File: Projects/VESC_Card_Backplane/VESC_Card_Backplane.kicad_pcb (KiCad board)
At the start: 2 copper layers, 82 x 131 mm, 202 parts, among them M1 FE1.1S, P1 USB_OTG, P10 AMP17614426-2_EDGE, P11 CONN_01X06, P12 CONN_01X02, P13 CONN_01X02, P14 CONN_01X02, P2 EC90_Flat, P3 AMP17614426-2_EDGE, P4 CONN_01X06, P5 CONN_01X04, P5V1 CONN_01X02, P6 EC90_Flat, P7 AMP17614426-2_EDGE, P8 CONN_01X06, P9 EC90_Flat

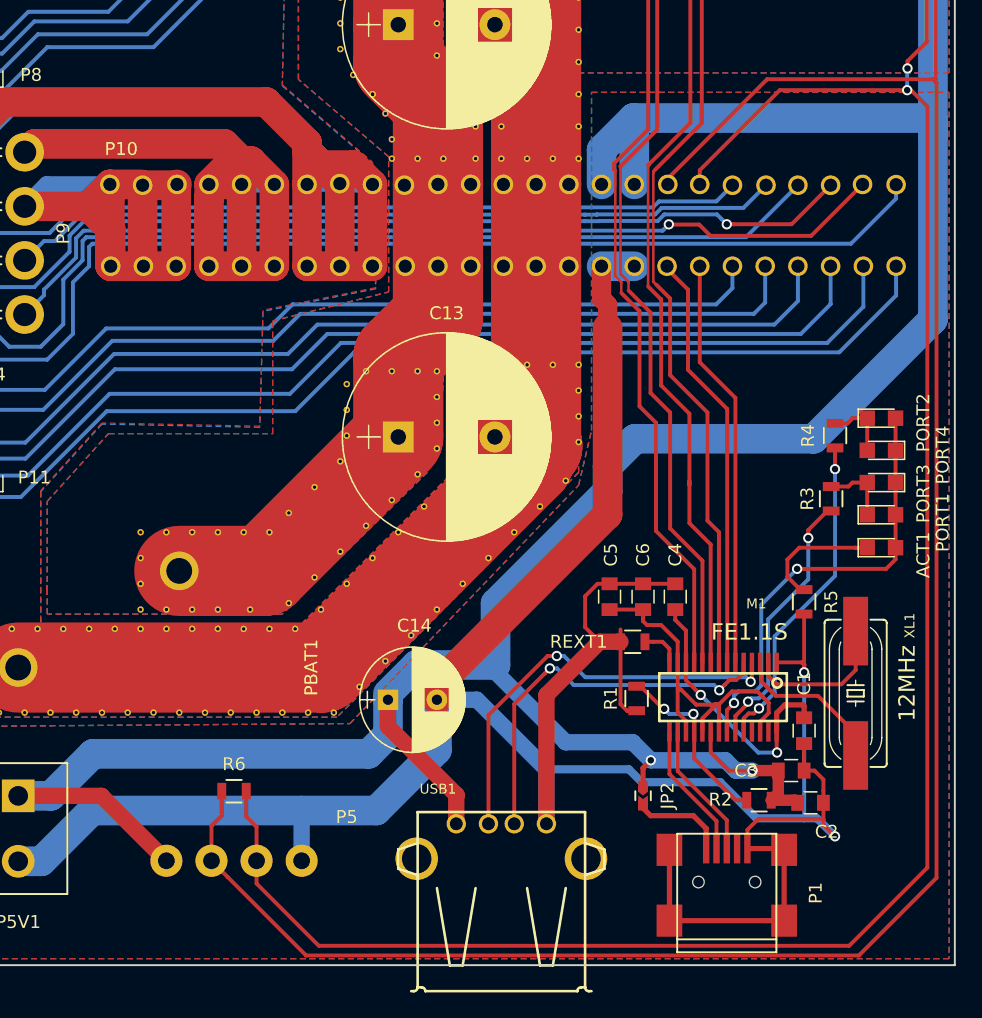
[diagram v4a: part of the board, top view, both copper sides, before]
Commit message: Finished connecting the components, just need to fix copper zones
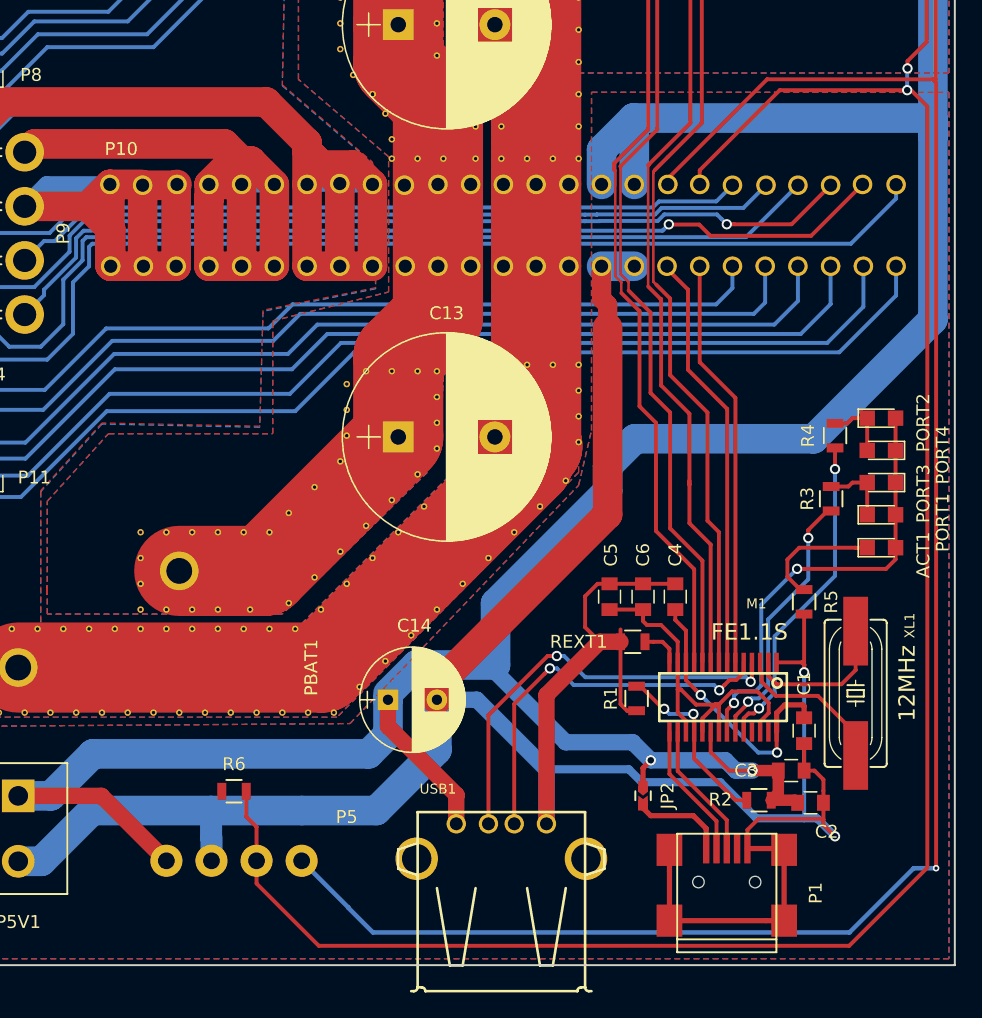
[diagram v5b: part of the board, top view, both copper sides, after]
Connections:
- P5 pad 2: /CANH -> GND
- P5 pad 4: GND -> /CANH
- R6 pad 1: /CANH -> GND
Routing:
- net /CANH: track 261.8 -> 247.1 mm, vias 0 -> 1
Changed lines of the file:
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@@
-(kicad_pcb (version 4) (host pcbnew 4.0.5)
+(kicad_pcb (version 4) (host pcbnew 4.0.4-stable)
   (general
-    (links 416)
-    (no_connects 41)
+    (links 382)
+    (no_connects 7)
     (area 28.124999 14.524999 110.275001 145.675001)
     (thickness 1.6)
     (drawings 8)
-    (tracks 1061)
+    (tracks 1064)
     (zones 0)
     (modules 202)
@@
       (net 3 +5V))
     (pad 2 thru_hole circle (at 3.5 0) (size 2.5 2.5) (drill 1.3) (layers *.Cu *.Mask)
-      (net 32 /CANH))
+      (net 2 GND))
     (pad 3 thru_hole circle (at 7 0) (size 2.5 2.5) (drill 1.3) (layers *.Cu *.Mask)
       (net 33 /CAN_Bus/CANL))
     (pad 4 thru_hole circle (at 10.5 0) (size 2.5 2.5) (drill 1.3) (layers *.Cu *.Mask)
-      (net 2 GND))
+      (net 32 /CANH))
   )
   (module USST-footprints:Molex_39531_1002 (layer F.Cu)
@@
     (fp_line (start -0.6 -0.875) (end 0.6 -0.875) (layer F.SilkS) (width 0.15))
     (pad 1 smd rect (at -0.95 0) (size 0.7 1.3) (layers F.Cu F.Paste F.Mask)
-      (net 32 /CANH))
+      (net 2 GND))
     (pad 2 smd rect (at 0.95 0) (size 0.7 1.3) (layers F.Cu F.Paste F.Mask)
       (net 33 /CAN_Bus/CANL))
@@
   (segment (start 98.4064 125.4) (end 98.5 125.4936) (width 0.4064) (layer F.Cu) (net 1))
   (segment (start 98.5 125.4936) (end 98.5 126.4) (width 0.4064) (layer F.Cu) (net 1))
+  (segment (start 43.236051 133.6) (end 52.47 133.6) (width 2.3) (layer B.Cu) (net 2))
+  (segment (start 52.5 137.5) (end 52.5 135.732234) (width 1.71) (layer B.Cu) (net 2))
+  (segment (start 52.47 133.6) (end 59.5 133.6) (width 2.3) (layer B.Cu) (net 2))
+  (segment (start 52.5 135.732234) (end 52.47 135.702234) (width 1.27) (layer B.Cu) (net 2))
+  (segment (start 52.47 135.702234) (end 52.47 133.6) (width 1.71) (layer B.Cu) (net 2))
   (segment (start 83.25 94.35) (end 82.78 93.88) (width 1.5) (layer F.Cu) (net 2))
   (segment (start 82.78 93.88) (end 82.78 91.35) (width 1.5) (layer F.Cu) (net 2))
@@
   (segment (start 65.3 133.6) (end 70 128.9) (width 2.3) (layer B.Cu) (net 2))
   (segment (start 59.5 133.6) (end 65.3 133.6) (width 2.3) (layer B.Cu) (net 2))
-  (segment (start 43.236051 133.6) (end 59.5 133.6) (width 2.3) (layer B.Cu) (net 2))
   (segment (start 39.296051 137.54) (end 43.236051 133.6) (width 2.3) (layer B.Cu) (net 2))
   (segment (start 37.5 137.54) (end 39.296051 137.54) (width 2.3) (layer B.Cu) (net 2))
@@
   (segment (start 84.25 125.343227) (end 84.756773 125.85) (width 0.3048) (layer F.Cu) (net 2))
   (segment (start 84.756773 125.85) (end 85.5 125.85) (width 0.3048) (layer F.Cu) (net 2))
-  (segment (start 59.5 133.6) (end 59.5 137.5) (width 1.27) (layer B.Cu) (net 2))
   (segment (start 78.5001 130.4001) (end 73.1 125) (width 1.27) (layer B.Cu) (net 2))
   (segment (start 73.1 125) (end 70 125) (width 1.27) (layer B.Cu) (net 2))
@@
   (segment (start 57.5 28.85) (end 57.5 22.5) (width 2.3) (layer F.Cu) (net 31))
   (segment (start 54.96 28.85) (end 54.96 22.5) (width 2.3) (layer F.Cu) (net 31))
-  (segment (start 108.5 76.8385) (end 108.778457 77.116957) (width 0.3048) (layer F.Cu) (net 32))
-  (segment (start 108.778457 77.116957) (end 108.778457 138.821543) (width 0.3048) (layer F.Cu) (net 32))
-  (segment (start 108.778457 138.821543) (end 102.75 144.85) (width 0.3048) (layer F.Cu) (net 32))
-  (segment (start 102.75 144.85) (end 59.85 144.85) (width 0.3048) (layer F.Cu) (net 32))
-  (segment (start 59.85 144.85) (end 53.749999 138.749999) (width 0.3048) (layer F.Cu) (net 32))
-  (segment (start 53.749999 138.749999) (end 52.5 137.5) (width 0.3048) (layer F.Cu) (net 32))
+  (segment (start 108.744286 138.077126) (end 107.007126 138.077126) (width 0.35) (layer B.Cu) (net 32))
+  (segment (start 107.007126 138.077126) (end 102.024252 143.06) (width 0.35) (layer B.Cu) (net 32))
+  (segment (start 102.024252 143.06) (end 65.034652 143.06) (width 0.35) (layer B.Cu) (net 32))
+  (segment (start 63.11815 141.11815) (end 59.5 137.5) (width 0.35) (layer B.Cu) (net 32))
+  (segment (start 65.034652 143.06) (end 63.11815 141.143498) (width 0.35) (layer B.Cu) (net 32))
+  (segment (start 63.11815 141.143498) (end 63.11815 141.11815) (width 0.35) (layer B.Cu) (net 32))
+  (via (at 108.744286 138.077126) (size 0.508) (drill 0.254) (layers F.Cu B.Cu) (net 32))
+  (segment (start 108.5 76.8385) (end 108.744286 77.082786) (width 0.3048) (layer F.Cu) (net 32))
+  (segment (start 108.744286 77.082786) (end 108.744286 138.077126) (width 0.3048) (layer F.Cu) (net 32))
   (segment (start 108.5 76.8385) (end 108.716735 76.8385) (width 0.3048) (layer F.Cu) (net 32))
   (segment (start 108.716735 76.8385) (end 108.716735 48.85) (width 0.3048) (layer F.Cu) (net 32))
@@
   (segment (start 87.9235 84.546156) (end 95.631156 76.8385) (width 0.3048) (layer F.Cu) (net 32))
   (segment (start 95.631156 76.8385) (end 108.5 76.8385) (width 0.3048) (layer F.Cu) (net 32))
-  (segment (start 52.5 137.5) (end 52.5 134.8) (width 0.3048) (layer F.Cu) (net 32))
-  (segment (start 52.5 134.8) (end 53.3 134) (width 0.3048) (layer F.Cu) (net 32))
-  (segment (start 53.3 134) (end 53.3 132.1) (width 0.3048) (layer F.Cu) (net 32))
   (segment (start 90.4 85) (end 90.4 83.896797) (width 0.3048) (layer F.Cu) (net 33))
   (segment (start 90.4 83.896797) (end 96.612047 77.68475) (width 0.3048) (layer F.Cu) (net 33))

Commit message: sync for working with liz
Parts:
- added G***: LOGO, USST-footprints:USSTLOGO, F.Cu at (94.8, 39.2)
- added G***: LOGO, USST-footprints:OSH_PARK_LOGO_SM, F.Cu at (107.5, 134.6)
- added REF**: VIA_STICH_0.5, USST-footprints:VIA_STICH_0.5, F.Cu at (67.5, 20.5)
- added REF**: VIA_STICH_0.5, USST-footprints:VIA_STICH_0.5, F.Cu at (73.2, 50.5)
- added REF**: VIA_STICH_0.5, USST-footprints:VIA_STICH_0.5, F.Cu at (73.2, 49.2)
- added REF**: VIA_STICH_0.5, USST-footprints:VIA_STICH_0.5, F.Cu at (72.2, 48.0)
- added REF**: VIA_STICH_0.5, USST-footprints:VIA_STICH_0.5, F.Cu at (71.2, 46.8)
- added REF**: VIA_STICH_0.5, USST-footprints:VIA_STICH_0.5, F.Cu at (70.0, 45.5)
- added REF**: VIA_STICH_0.5, USST-footprints:VIA_STICH_0.5, F.Cu at (70.0, 44.0)
- added REF**: VIA_STICH_0.5, USST-footprints:VIA_STICH_0.5, F.Cu at (70.0, 42.5)
- added REF**: VIA_STICH_0.5, USST-footprints:VIA_STICH_0.5, F.Cu at (70.0, 40.8)
- added REF**: VIA_STICH_0.5, USST-footprints:VIA_STICH_0.5, F.Cu at (70.0, 39.2)
- added REF**: VIA_STICH_0.5, USST-footprints:VIA_STICH_0.5, F.Cu at (71.2, 38.0)
- added REF**: VIA_STICH_0.5, USST-footprints:VIA_STICH_0.5, F.Cu at (69.5, 20.5)
- added REF**: VIA_STICH_0.5, USST-footprints:VIA_STICH_0.5, F.Cu at (72.5, 36.8)
- added REF**: VIA_STICH_0.5, USST-footprints:VIA_STICH_0.5, F.Cu at (73.2, 35.5)
- added REF**: VIA_STICH_0.5, USST-footprints:VIA_STICH_0.5, F.Cu at (71.0, 35.5)
- added REF**: VIA_STICH_0.5, USST-footprints:VIA_STICH_0.5, F.Cu at (69.5, 35.5)
- added REF**: VIA_STICH_0.5, USST-footprints:VIA_STICH_0.5, F.Cu at (67.5, 35.5)
- added REF**: VIA_STICH_0.5, USST-footprints:VIA_STICH_0.5, F.Cu at (65.8, 35.5)
- added REF**: VIA_STICH_0.5, USST-footprints:VIA_STICH_0.5, F.Cu at (64.0, 36.5)
- added REF**: VIA_STICH_0.5, USST-footprints:VIA_STICH_0.5, F.Cu at (62.2, 37.5)
- added REF**: VIA_STICH_0.5, USST-footprints:VIA_STICH_0.5, F.Cu at (61.0, 38.5)
- added REF**: VIA_STICH_0.5, USST-footprints:VIA_STICH_0.5, F.Cu at (60.0, 39.8)
- added REF**: VIA_STICH_0.5, USST-footprints:VIA_STICH_0.5, F.Cu at (71.2, 20.5)
- added REF**: VIA_STICH_0.5, USST-footprints:VIA_STICH_0.5, F.Cu at (60.0, 41.2)
- added REF**: VIA_STICH_0.5, USST-footprints:VIA_STICH_0.5, F.Cu at (60.0, 42.5)
- added REF**: VIA_STICH_0.5, USST-footprints:VIA_STICH_0.5, F.Cu at (60.0, 44.0)
- added REF**: VIA_STICH_0.5, USST-footprints:VIA_STICH_0.5, F.Cu at (60.0, 45.5)
- added REF**: VIA_STICH_0.5, USST-footprints:VIA_STICH_0.5, F.Cu at (61.2, 46.8)
- added REF**: VIA_STICH_0.5, USST-footprints:VIA_STICH_0.5, F.Cu at (62.5, 48.0)
- added REF**: VIA_STICH_0.5, USST-footprints:VIA_STICH_0.5, F.Cu at (64.0, 49.2)
- added REF**: VIA_STICH_0.5, USST-footprints:VIA_STICH_0.5, F.Cu at (65.2, 50.5)
- added REF**: VIA_STICH_0.5, USST-footprints:VIA_STICH_0.5, F.Cu at (66.8, 51.8)
- added REF**: VIA_STICH_0.5, USST-footprints:VIA_STICH_0.5, F.Cu at (67.5, 53.0)
- added REF**: VIA_STICH_0.5, USST-footprints:VIA_STICH_0.5, F.Cu at (73.0, 20.5)
- added REF**: VIA_STICH_0.5, USST-footprints:VIA_STICH_0.5, F.Cu at (69.5, 53.0)
- added REF**: VIA_STICH_0.5, USST-footprints:VIA_STICH_0.5, F.Cu at (71.2, 53.0)
- added REF**: VIA_STICH_0.5, USST-footprints:VIA_STICH_0.5, F.Cu at (73.0, 53.0)
- added REF**: VIA_STICH_0.5, USST-footprints:VIA_STICH_0.5, F.Cu at (67.5, 62.8)
- added REF**: VIA_STICH_0.5, USST-footprints:VIA_STICH_0.5, F.Cu at (69.0, 62.8)
- added REF**: VIA_STICH_0.5, USST-footprints:VIA_STICH_0.5, F.Cu at (70.2, 62.8)
- added REF**: VIA_STICH_0.5, USST-footprints:VIA_STICH_0.5, F.Cu at (71.5, 62.8)
- added REF**: VIA_STICH_0.5, USST-footprints:VIA_STICH_0.5, F.Cu at (72.8, 62.8)
- added REF**: VIA_STICH_0.5, USST-footprints:VIA_STICH_0.5, F.Cu at (67.2, 30.5)
- added REF**: VIA_STICH_0.5, USST-footprints:VIA_STICH_0.5, F.Cu at (69.0, 30.5)
- added REF**: VIA_STICH_0.5, USST-footprints:VIA_STICH_0.5, F.Cu at (71.0, 30.5)
- added REF**: VIA_STICH_0.5, USST-footprints:VIA_STICH_0.5, F.Cu at (72.8, 30.5)
- added REF**: VIA_STICH_0.5, USST-footprints:VIA_STICH_0.5, F.Cu at (73.2, 51.8)
- moved R6 3.31 mm to (57.5, 132.8)
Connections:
- R6 pad 1: GND -> /CAN_Bus/CANL
- R6 pad 2: /CAN_Bus/CANL -> /CANH
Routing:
- net /CANH: track 247.1 -> 255.0 mm
- net /CAN_Bus/CANL: track 246.1 -> 247.3 mm, vias 4 -> 5
- net /Motor_Controller_C/H3: track 71.1 -> 71.8 mm
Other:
- board size 82 x 131 mm -> 82 x 129.8 mm
- board text added: "2017"
- board text added: "VESC-R Backplane"

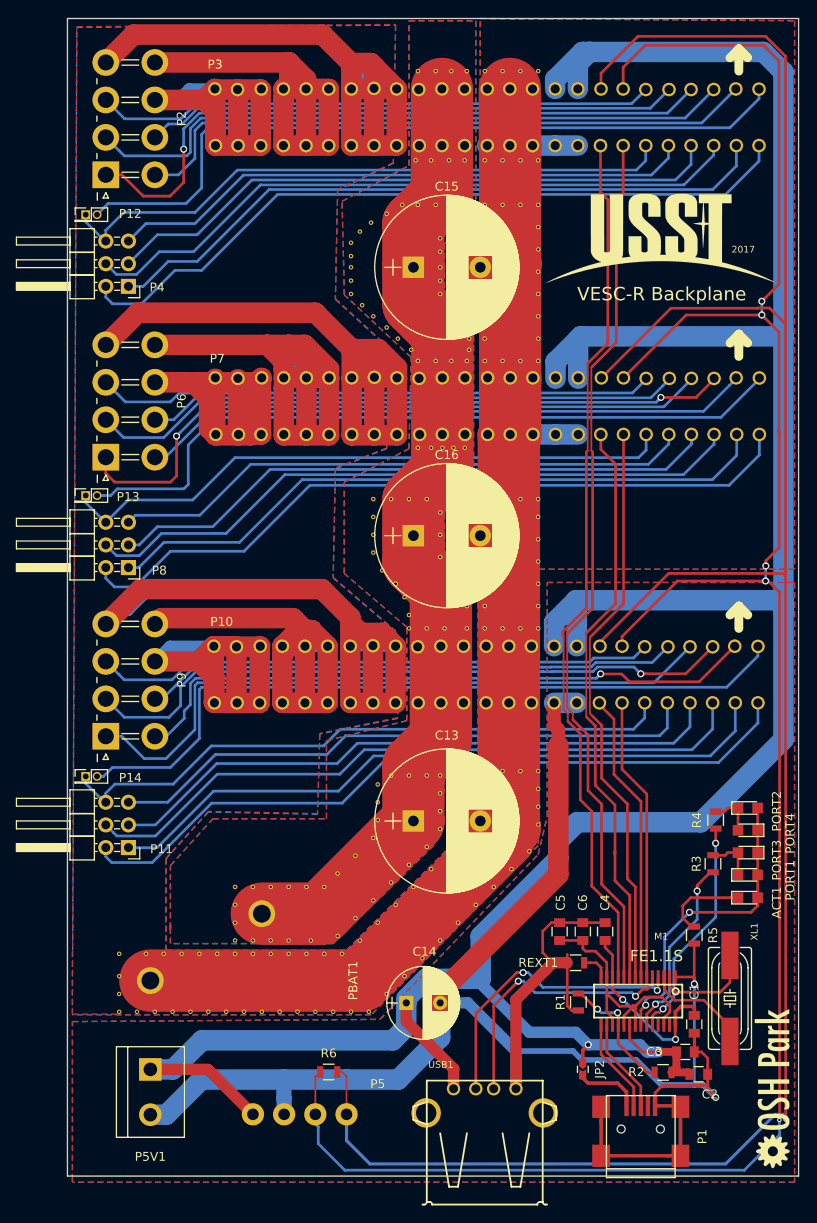
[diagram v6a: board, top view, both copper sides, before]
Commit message: Added copper zones in VESC Backplane
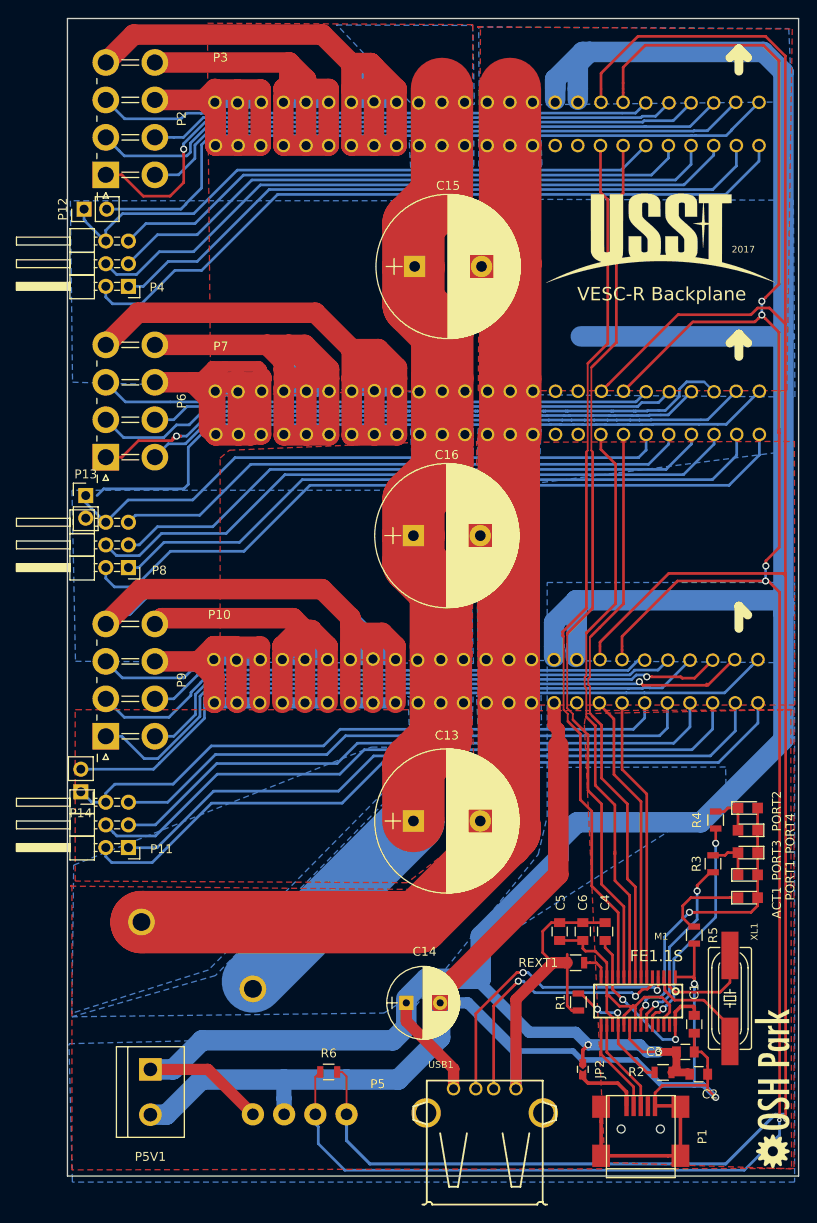
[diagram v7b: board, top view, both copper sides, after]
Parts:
- removed REF** (x207): VIA_STICH_0.5, USST-footprints:VIA_STICH_0.5
- P10, P3, P7: footprint USST-footprints:TE2007088-1_Backplane -> USST-footprints:TE2007088-1_Backplane2
- P12, P13, P14: footprint Pin_Headers:Pin_Header_Straight_2x01_Pitch1.27mm -> Pin_Headers:Pin_Header_Straight_1x02_Pitch2.54mm
- PBAT1: moved to B.Cu
- moved PBAT1 6.65 mm to (36.5, 115.9), turned to 270 degrees
- moved P14 1.82 mm to (29.7, 101.3), turned to 180 degrees
- moved P12 0.65 mm to (30.1, 36.0), turned to 90 degrees
- moved C15 0.17 mm to (67.1, 42.4)
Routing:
- net /Motor_Controller_B/X: track 91.7 -> 117.6 mm
- net /Motor_Controller_C/Y: track 116.1 -> 133.5 mm
- net /Motor_Controller_C/X: track 84.8 -> 100.9 mm
- net /VBAT: track 110.0 -> 125.9 mm
- net /Motor_Controller_B/W: track 61.9 -> 74.2 mm
- net /Motor_Controller_A/Y: track 120.2 -> 132.3 mm
- net /Motor_Controller_A/X: track 84.6 -> 95.9 mm
- net /Motor_Controller_B/Y: track 120.6 -> 131.2 mm
- net /Motor_Controller_B/H1: track 75.3 -> 69.8 mm
- net /PGND: track 228.6 -> 223.3 mm
- net +5V: track 346.6 -> 341.8 mm
- net /CAN_Bus/CANL: track 247.3 -> 250.9 mm
- net /CANH: track 255.0 -> 258.6 mm
- net Net-(P12-Pad2): track 84.2 -> 81.0 mm
- net GND: track 219.2 -> 216.7 mm
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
